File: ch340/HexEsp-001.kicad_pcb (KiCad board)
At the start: 2 copper layers, 49 x 43 mm, 29 parts, among them IC1 CH340G, J1 1x6_female_pin_Header_2.54mm, J2 1x6_female_pin_Header_2.54mm, J3 1x6_female_pin_Header_2.54mm, J4 1x6_female_pin_Header_2.54mm, Q1 PZT2222A, Q2 PZT2222A, U1 ESP-12E, U2 SPX3819, U3 PUSHBUTTON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

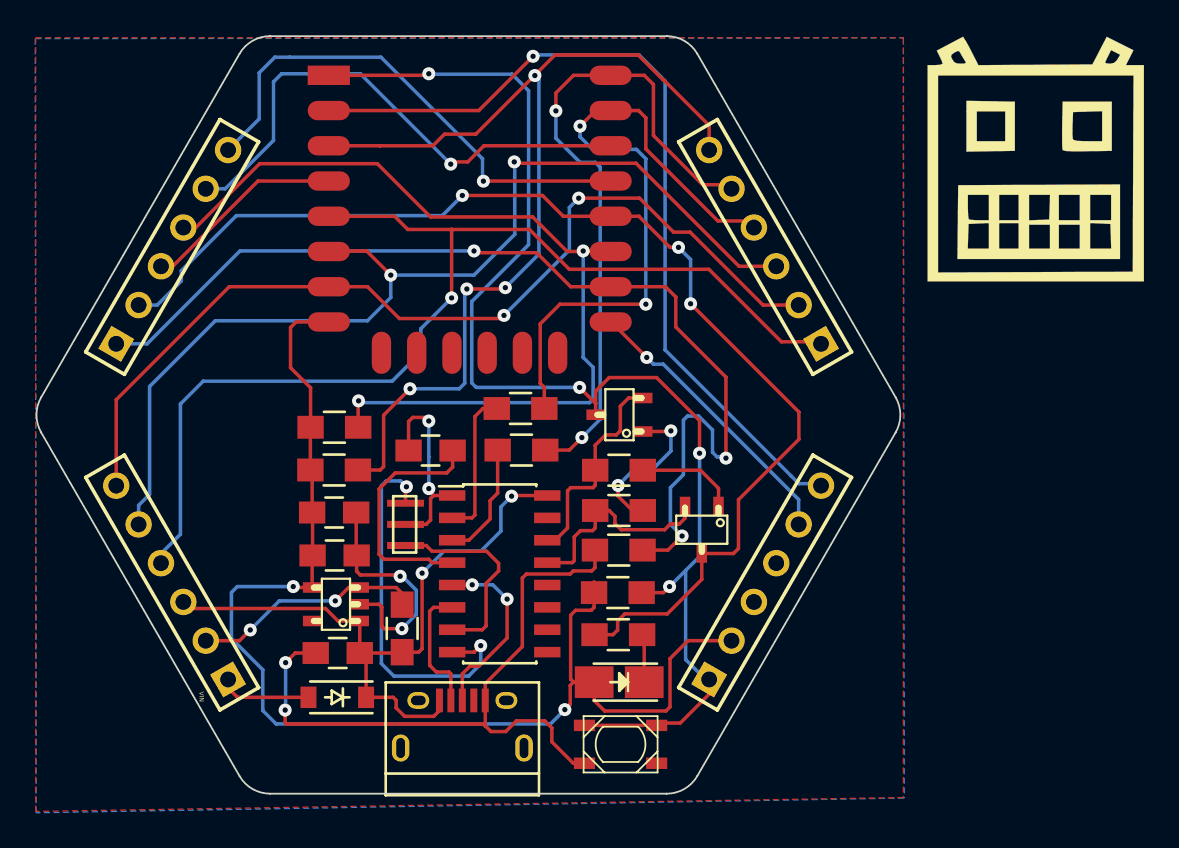
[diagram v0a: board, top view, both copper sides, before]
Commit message: Re-organized directory
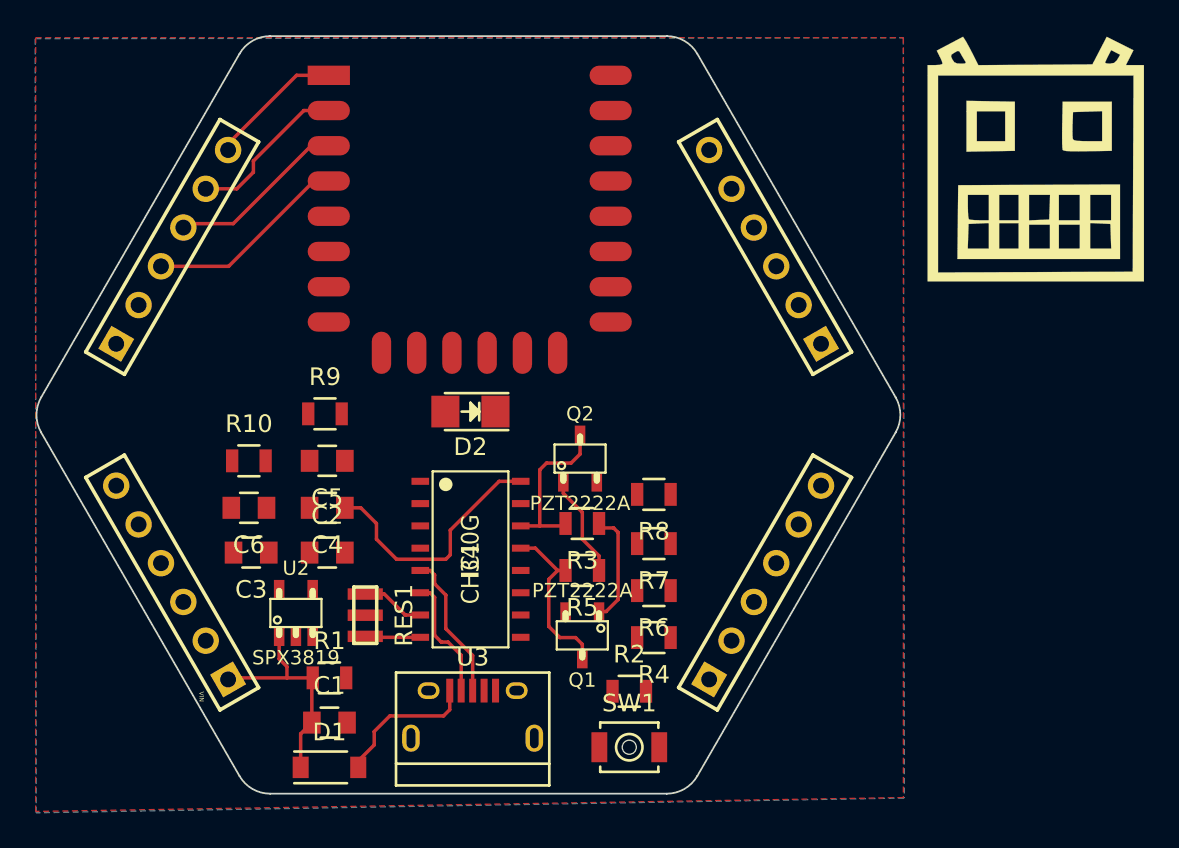
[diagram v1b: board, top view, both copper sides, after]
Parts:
- removed D3: PURPLE, GTB2:LED_1206_Hand_Soldering
- removed R12, R13: 470, Resistors_SMD:R_0805_HandSoldering
- removed U4: MICRO-B_USB, Connect:USB_Micro-B
- added C5: 100nF, Capacitors_SMD:C_0805, F.Cu at (134.0, 60.3)
- added C6: 100nF, Capacitors_SMD:C_0805, F.Cu at (129.5, 63.0)
- added D2: PURPLE, LEDs:LED_1206, F.Cu at (142.1, 57.5)
- added R10: 470, Resistors_SMD:R_0805, F.Cu at (129.5, 60.3)
- added R2: 10K, Resistors_SMD:R_0805, F.Cu at (151.1, 73.4)
- added SW1: RESET, Buttons_Switches_SMD:SW_SPST_B3U-1000P-B, F.Cu at (151.1, 76.6)
- C1, C4: footprint Capacitors_SMD:C_0805_HandSoldering -> Capacitors_SMD:C_0805
- C2: value 1uF -> 10uF; footprint Capacitors_SMD:C_0805_HandSoldering -> Capacitors_SMD:C_0805
- C3: value 10uF -> 1uF; footprint Capacitors_SMD:C_0805_HandSoldering -> Capacitors_SMD:C_0805
- IC1: footprint Housings_SOIC:SOIC-16_3.9x9.9mm_Pitch1.27mm -> CH340G:SOP-16
- Q1, Q2: footprint MazEsp-001:AB2_SOT23-3 -> ab2_sot:AB2_SOT23-3
- R1, R3, R4, R6: footprint Resistors_SMD:R_0805_HandSoldering -> Resistors_SMD:R_0805
- R5: value 1K -> 10K; footprint Resistors_SMD:R_0805_HandSoldering -> Resistors_SMD:R_0805
- R7, R8: value 10K -> 1K; footprint Resistors_SMD:R_0805_HandSoldering -> Resistors_SMD:R_0805
- R9: value 1K -> 470; footprint Resistors_SMD:R_0805_HandSoldering -> Resistors_SMD:R_0805
- RES1: footprint makerlab:RESONATOR_CSTCE -> Resonators:murata-resonator_SMD_CSTCE8M00G55-R0
- U2: footprint AB2_SOT23-5 -> ab2_sot:AB2_SOT23-5
- U3: value PUSHBUTTON -> MICRO-B_USB; footprint makerlab:PUSHBUTTON_SMD_PTS810 -> Connect:USB_Micro-B
- moved R4 21.7 mm to (152.5, 70.4)
- moved R9 20.8 mm to (133.9, 57.7)
- moved R5 15.2 mm to (148.5, 66.5)
- moved Q1 9.05 mm to (148.5, 70.2)
- moved U3 8.53 mm to (142.2, 74.9), turned to 0 degrees
- moved C4 6.71 mm to (134.0, 63.0)
- moved RES1 5.64 mm to (136.1, 69.1), turned to 270 degrees
- moved C3 5.23 mm to (129.7, 65.5), turned to 180 degrees
- moved R1 4.99 mm to (134.1, 72.6), turned to 0 degrees
- moved R7 4.61 mm to (152.5, 65.0)
- moved R3 4.41 mm to (148.5, 63.9), turned to 180 degrees
- moved D1 4.00 mm to (134.1, 77.7), turned to 0 degrees
- moved C1 3.98 mm to (134.1, 75.2), turned to 0 degrees
- moved Q2 3.35 mm to (148.3, 60.2), turned to 0 degrees
- moved R6 3.04 mm to (152.5, 67.7), turned to 180 degrees
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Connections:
- C4 pad 1: Net-(C4-Pad1) -> VBUS
- D1 pad 2: VIN -> VBUS
- IC1 pad 4: Net-(C4-Pad1) -> Net-(C5-Pad1)
- J1 pad 1: /GPIO15 -> GND
- J1 pad 2: /GPIO0 -> /GPIO12
- J1 pad 4: /GPIO2 -> /CH_PD
- J1 pad 5: /GPIO5 -> /ADC
- J1 pad 6: /GPIO4 -> /RESET
- J2 pad 1: VIN -> VBUS
- J2 pad 2: /EN -> +3V3
- J2 pad 3: VBUS -> GND
- J2 pad 4: /GPIO14 -> /GPIO13
- J2 pad 6: /GPIO13 -> /GPIO14
- J3 pad 1: /GPIO14 -> /GPIO2
- J3 pad 2: /GPIO13 -> /GPIO0
- J3 pad 3: /GPIO12 -> /GPIO4
- J3 pad 4: /RXD -> /GPIO5
- J3 pad 5: /TXD -> /RXD
- J3 pad 6: /CH_PD -> /TXD
- J4 pad 1: /RESET -> VBUS
- J4 pad 2: +3V3 -> Net-(J4-Pad2)
- J4 pad 4: GND -> +3V3
- J4 pad 6: /ADC -> /GPIO15
- R3 pad 1: +3V3 -> Net-(Q1-Pad1)
- R3 pad 2: /RESET -> /RTS
- R5 pad 1: /CH_PD -> Net-(Q2-Pad1)
- R5 pad 2: +3V3 -> /DTR
- R6 pad 1: GND -> /CH_PD
- R6 pad 2: /GPIO15 -> +3V3
- R7 pad 1: Net-(Q1-Pad1) -> GND
- R7 pad 2: /RTS -> /GPIO15
- R8 pad 1: Net-(Q2-Pad1) -> /GPIO0
- R8 pad 2: /DTR -> Net-(D2-Pad1)
- R9 pad 1: /GPIO0 -> /RXD
- R9 pad 2: Net-(D3-Pad1) -> Net-(IC1-Pad2)
- U2 pad 4: +3V3 -> Net-(U2-Pad4)
- U2 pad 5: Net-(U2-Pad5) -> +3V3
- U3 pad 1: GND -> VBUS
- U3 pad 2: GND -> /D-
- U3 pad 3: /RESET -> /D+
- U3 pad 4: /RESET -> Net-(U3-Pad4)
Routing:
- net GND: track 79.8 -> 0.00 mm, vias 7 -> 0
- net +3V3: track 70.3 -> 0.00 mm, vias 2 -> 0
- net /GPIO0: track 67.5 -> 0.00 mm, vias 3 -> 0
- net /RESET: track 73.1 -> 7.68 mm, vias 4 -> 0
- net /GPIO14: track 63.1 -> 0.00 mm, vias 1 -> 0
- net /GPIO15: track 59.9 -> 0.00 mm, vias 3 -> 0
- net /GPIO12: track 58.7 -> 0.00 mm, vias 2 -> 0
- net /GPIO13: track 53.8 -> 0.00 mm, vias 2 -> 0
- net /GPIO2: track 51.5 -> 0.00 mm, vias 2 -> 0
- net /CH_PD: track 57.5 -> 10.2 mm, vias 4 -> 0
- net /ADC: track 48.3 -> 9.20 mm, vias 1 -> 0
- net /TXD: track 38.7 -> 0.00 mm, vias 2 -> 0
- net /RXD: track 38.5 -> 0.00 mm, vias 2 -> 0
- net /GPIO5: track 30.2 -> 0.00 mm, vias 1 -> 0
- net /GPIO4: track 29.1 -> 0.00 mm, vias 1 -> 0
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
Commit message: Some litle changes
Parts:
- removed SW1: RESET, Buttons_Switches_SMD:SW_SPST_B3U-1000P-B
- D1: value MBR120 -> PURPLE; footprint Diodes_SMD:SOD-123 -> LEDs:LED_1206
- D2: value PURPLE -> MBR120; footprint LEDs:LED_1206 -> Diodes_SMD:SOD-123
- R3: value 10K -> 1K
- R4: value 1K -> 10K
- moved R7 21.4 mm to (132.2, 58.4)
- moved D1 21.1 mm to (142.6, 58.4)
- moved D2 20.6 mm to (134.0, 76.5), turned to 0 degrees
- moved Q1 10.5 mm to (149.7, 59.8), turned to 0 degrees
- moved Q2 9.65 mm to (149.9, 69.7), turned to 180 degrees
- moved C5 7.87 mm to (135.4, 68.1)
- moved R4 7.36 mm to (149.9, 63.5)
- moved R10 6.77 mm to (136.3, 61.1)
- moved R3 6.54 mm to (154.2, 60.7)
- moved C2 6.39 mm to (127.9, 63.6)
- moved C3 4.79 mm to (127.9, 61.1), turned to 0 degrees
- moved RES1 4.59 mm to (136.5, 64.5)
- moved R6 4.50 mm to (154.2, 63.5), turned to 0 degrees
- moved R8 4.27 mm to (154.2, 66.2)
- moved C6 3.38 mm to (132.3, 61.1)
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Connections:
- D1 pad 1: VBUS -> Net-(D1-Pad1)
- D1 pad 2: VBUS -> +3V3
- D2 pad 1: Net-(D2-Pad1) -> VBUS
- D2 pad 2: +3V3 -> VBUS
- J1 pad 1: GND -> Net-(J1-Pad1)
- J1 pad 2: /GPIO12 -> Net-(J1-Pad2)
- R3 pad 1: Net-(Q1-Pad1) -> /GPIO0
- R3 pad 2: /RTS -> Net-(D1-Pad1)
- R4 pad 1: /GPIO2 -> Net-(Q1-Pad1)
- R4 pad 2: +3V3 -> /RTS
- R6 pad 1: /CH_PD -> /GPIO2
- R7 pad 1: GND -> /CH_PD
- R7 pad 2: /GPIO15 -> +3V3
- R8 pad 1: /GPIO0 -> GND
- R8 pad 2: Net-(D2-Pad1) -> /GPIO15
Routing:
- net VBUS: track 35.4 -> 0.00 mm
- net /GPIO16: track 11.5 -> 0.97 mm
- net /DTR: track 9.62 -> 0.00 mm
- net /RTS: track 9.54 -> 0.00 mm
- net /ADC: track 9.20 -> 0.00 mm
- net /CH_PD: track 10.2 -> 1.00 mm
- net /D+: track 8.38 -> 0.00 mm
- net /RESET: track 7.68 -> 0.00 mm
- net /D-: track 7.06 -> 0.00 mm
- net Net-(Q1-Pad1): track 6.47 -> 0.00 mm
- net Net-(Q2-Pad1): track 5.84 -> 0.00 mm
- net /XI: track 3.62 -> 0.00 mm
- net /XO: track 3.15 -> 0.00 mm
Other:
- net class Default: clearance 0.2 -> 0.149; trace_width 0.2 -> 0.15; via_dia 0.74 -> 0.6
- rule trace_clearance: 0.2 -> 0.149
- rule trace_min: 0.2 -> 0.15
- rule via_min_size: 0.64 -> 0.6
